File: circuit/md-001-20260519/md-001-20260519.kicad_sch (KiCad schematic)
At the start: 41 parts, among them J1 VIN-motor, J2 Conn_Ball_Catch, J3 Conn_relay

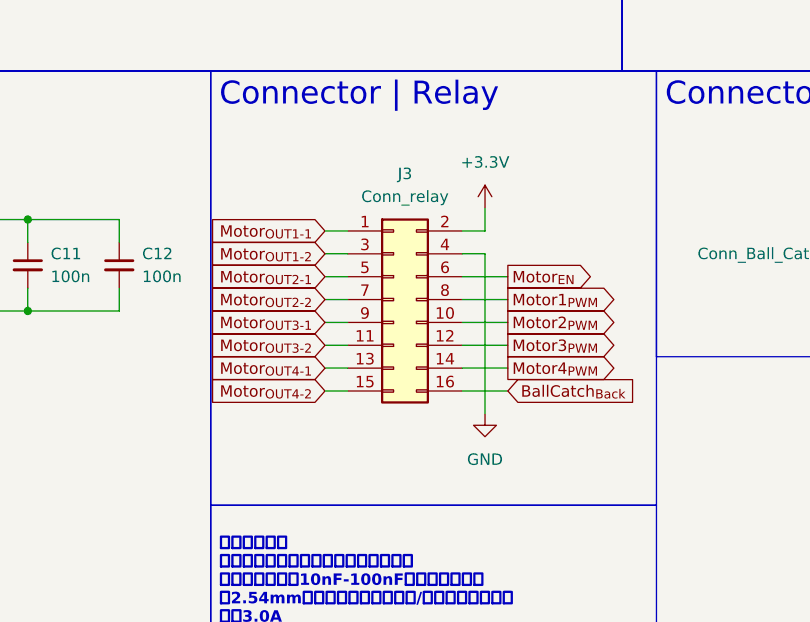
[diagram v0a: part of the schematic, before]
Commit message: Update MD基板のピンソケット→ピンヘッダへの修正を完了させた
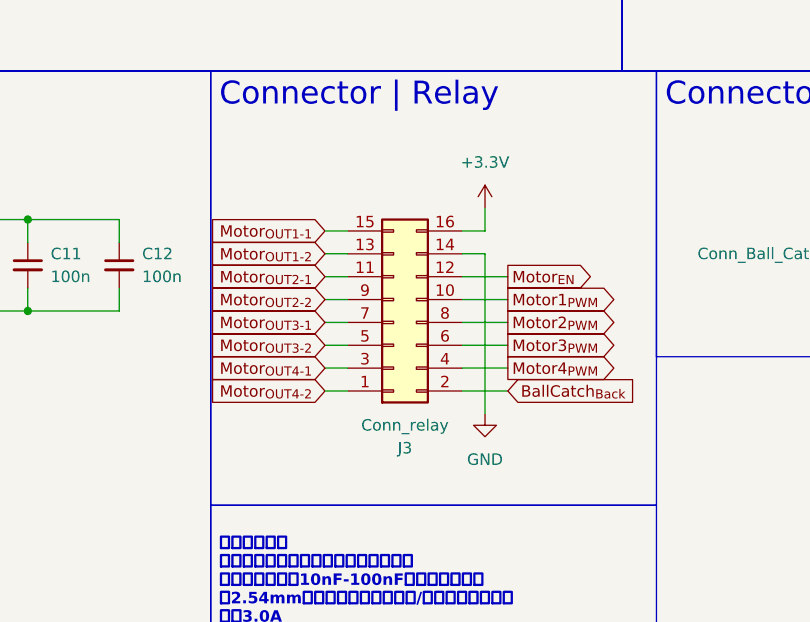
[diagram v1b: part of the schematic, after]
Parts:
- J3: footprint Connector_PinSocket_2.54mm:PinSocket_2x08_P2.54mm_Horizontal -> Connector_PinHeader_2.54mm:PinHeader_2x08_P2.54mm_Horizontal
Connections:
- net +3.3V: now also J3.16 (Pin_16); no longer J3.2 (Pin_2)
- net BallCatch_{Back}: now also J3.2 (Pin_2); no longer J3.16 (Pin_16)
- net GND: now also J3.14 (Pin_14); no longer J3.4 (Pin_4)
- net Motor1_{PWM}: now also J3.10 (Pin_10); no longer J3.8 (Pin_8)
- net Motor2_{PWM}: now also J3.8 (Pin_8); no longer J3.10 (Pin_10)
- net Motor3_{PWM}: now also J3.6 (Pin_6); no longer J3.12 (Pin_12)
- net Motor4_{PWM}: now also J3.4 (Pin_4); no longer J3.14 (Pin_14)
- net Motor_{EN}: now also J3.12 (Pin_12); no longer J3.6 (Pin_6)
- net Motor_{OUT1-1}: now also J3.15 (Pin_15); no longer J3.1 (Pin_1)
- net Motor_{OUT1-2}: now also J3.13 (Pin_13); no longer J3.3 (Pin_3)
- net Motor_{OUT2-1}: now also J3.11 (Pin_11); no longer J3.5 (Pin_5)
- net Motor_{OUT2-2}: now also J3.9 (Pin_9); no longer J3.7 (Pin_7)
- net Motor_{OUT3-1}: now also J3.7 (Pin_7); no longer J3.9 (Pin_9)
- net Motor_{OUT3-2}: now also J3.5 (Pin_5); no longer J3.11 (Pin_11)
- net Motor_{OUT4-1}: now also J3.3 (Pin_3); no longer J3.13 (Pin_13)
- net Motor_{OUT4-2}: now also J3.1 (Pin_1); no longer J3.15 (Pin_15)
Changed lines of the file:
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@@
 	(symbol
 		(lib_id "Connector_Generic:Conn_02x08_Odd_Even")
-		(at 101.6 144.78 0)
+		(at 101.6 147.32 0)
+		(mirror x)
 		(unit 1)
 		(body_style 1)
@@
 		(in_pos_files yes)
 		(dnp no)
-		(fields_autoplaced yes)
 		(property "Reference" "J3"
-			(at 102.87 130.81 0)
+			(at 102.87 161.29 0)
 			(show_name no)
 			(do_not_autoplace no)
@@
 		)
 		(property "Value" "Conn_relay"
-			(at 102.87 133.35 0)
+			(at 102.87 158.75 0)
 			(show_name no)
 			(do_not_autoplace no)
@@
 			)
 		)
-		(property "Footprint" "Connector_PinSocket_2.54mm:PinSocket_2x08_P2.54mm_Horizontal"
-			(at 101.6 144.78 0)
+		(property "Footprint" "Connector_PinHeader_2.54mm:PinHeader_2x08_P2.54mm_Horizontal"
+			(at 101.6 147.32 0)
 			(hide yes)
 			(show_name no)
@@
 		)
 		(property "Datasheet" ""
-			(at 101.6 144.78 0)
+			(at 101.6 147.32 0)
 			(hide yes)
 			(show_name no)
@@
 		)
 		(property "Description" "Generic connector, double row, 02x08, odd/even pin numbering scheme (row 1 odd numbers, row 2 even numbers), script generated (kicad-library-utils/schlib/autogen/connector/)"
-			(at 101.6 144.78 0)
+			(at 101.6 147.32 0)
 			(hide yes)
 			(show_name no)
